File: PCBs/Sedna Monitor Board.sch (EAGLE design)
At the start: 39 parts, among them J1 uC Connection

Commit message: Started working on the Monitor Board layout
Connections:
- net N$24: now also ADC.CH4; no longer ADC.CH1
- net N$4: now also ADC.CH0; no longer ADC.CH4
- net N$5: now also ADC.CH1; no longer ADC.CH0
- net N$8: now also ADC.CH3; no longer ADC.CH2
- net N$9: now also ADC.CH2; no longer ADC.CH3
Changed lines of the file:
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@@
 </instance>
 <instance part="GND1" gate="1" x="132.08" y="127" smashed="yes"/>
-<instance part="GND2" gate="1" x="116.84" y="101.6" smashed="yes"/>
+<instance part="GND2" gate="1" x="114.3" y="104.14" smashed="yes"/>
 <instance part="C5" gate="G$1" x="157.48" y="83.82" smashed="yes">
 <attribute name="NAME" x="156.21" y="87.503" size="1.778" layer="95"/>
@@
 <segment>
 <pinref part="TEMP_SENSE" gate="G$1" pin="VSS"/>
-<wire x1="119.38" y1="109.22" x2="116.84" y2="109.22" width="0.1524" layer="91"/>
-<wire x1="116.84" y1="109.22" x2="116.84" y2="104.14" width="0.1524" layer="91"/>
-<wire x1="116.84" y1="99.06" x2="116.84" y2="104.14" width="0.1524" layer="91"/>
+<wire x1="119.38" y1="109.22" x2="114.3" y2="109.22" width="0.1524" layer="91"/>
+<wire x1="114.3" y1="109.22" x2="114.3" y2="106.68" width="0.1524" layer="91"/>
 <pinref part="GND2" gate="1" pin="GND"/>
 </segment>
@@
 <segment>
 <pinref part="CURRENT_SENSE" gate="G$1" pin="OUT"/>
-<wire x1="119.38" y1="137.16" x2="106.68" y2="137.16" width="0.1524" layer="91"/>
-<wire x1="106.68" y1="137.16" x2="106.68" y2="71.12" width="0.1524" layer="91"/>
-<pinref part="ADC" gate="MCP3208" pin="CH4"/>
-<wire x1="106.68" y1="71.12" x2="119.38" y2="71.12" width="0.1524" layer="91"/>
+<wire x1="119.38" y1="137.16" x2="109.22" y2="137.16" width="0.1524" layer="91"/>
+<pinref part="ADC" gate="MCP3208" pin="CH0"/>
+<wire x1="109.22" y1="137.16" x2="109.22" y2="81.28" width="0.1524" layer="91"/>
+<wire x1="109.22" y1="81.28" x2="119.38" y2="81.28" width="0.1524" layer="91"/>
 </segment>
 </net>
@@
 <junction x="165.1" y="111.76"/>
 <pinref part="V_BUFFER" gate="G$1" pin="VDD"/>
-<wire x1="58.42" y1="73.66" x2="50.8" y2="73.66" width="0.1524" layer="91"/>
-<wire x1="50.8" y1="73.66" x2="50.8" y2="48.26" width="0.1524" layer="91"/>
-<wire x1="50.8" y1="48.26" x2="165.1" y2="48.26" width="0.1524" layer="91"/>
+<wire x1="58.42" y1="73.66" x2="48.26" y2="73.66" width="0.1524" layer="91"/>
+<wire x1="48.26" y1="73.66" x2="48.26" y2="48.26" width="0.1524" layer="91"/>
+<wire x1="48.26" y1="48.26" x2="165.1" y2="48.26" width="0.1524" layer="91"/>
 <wire x1="165.1" y1="48.26" x2="165.1" y2="86.36" width="0.1524" layer="91"/>
 <pinref part="J1" gate="G$1" pin="VCC"/>
@@
 <wire x1="149.86" y1="73.66" x2="185.42" y2="73.66" width="0.1524" layer="91"/>
 <pinref part="TEMP_SENSE" gate="G$1" pin="SCK"/>
-<wire x1="119.38" y1="106.68" x2="111.76" y2="106.68" width="0.1524" layer="91"/>
-<wire x1="111.76" y1="106.68" x2="111.76" y2="93.98" width="0.1524" layer="91"/>
-<wire x1="111.76" y1="93.98" x2="185.42" y2="93.98" width="0.1524" layer="91"/>
-<wire x1="185.42" y1="93.98" x2="185.42" y2="114.3" width="0.1524" layer="91"/>
+<wire x1="119.38" y1="106.68" x2="116.84" y2="106.68" width="0.1524" layer="91"/>
+<wire x1="116.84" y1="106.68" x2="116.84" y2="96.52" width="0.1524" layer="91"/>
+<wire x1="116.84" y1="96.52" x2="185.42" y2="96.52" width="0.1524" layer="91"/>
+<wire x1="185.42" y1="96.52" x2="185.42" y2="114.3" width="0.1524" layer="91"/>
 <wire x1="185.42" y1="114.3" x2="208.28" y2="114.3" width="0.1524" layer="91"/>
-<wire x1="185.42" y1="73.66" x2="185.42" y2="93.98" width="0.1524" layer="91"/>
-<junction x="185.42" y="93.98"/>
+<wire x1="185.42" y1="73.66" x2="185.42" y2="96.52" width="0.1524" layer="91"/>
+<junction x="185.42" y="96.52"/>
 <pinref part="J1" gate="G$1" pin="SCK"/>
 </segment>
@@
 <pinref part="TEMP_SENSE" gate="G$1" pin="SI/O"/>
 <wire x1="139.7" y1="106.68" x2="142.24" y2="106.68" width="0.1524" layer="91"/>
-<wire x1="142.24" y1="106.68" x2="142.24" y2="91.44" width="0.1524" layer="91"/>
-<wire x1="142.24" y1="91.44" x2="187.96" y2="91.44" width="0.1524" layer="91"/>
-<wire x1="187.96" y1="91.44" x2="187.96" y2="111.76" width="0.1524" layer="91"/>
+<wire x1="142.24" y1="106.68" x2="142.24" y2="99.06" width="0.1524" layer="91"/>
+<wire x1="142.24" y1="99.06" x2="187.96" y2="99.06" width="0.1524" layer="91"/>
+<wire x1="187.96" y1="99.06" x2="187.96" y2="111.76" width="0.1524" layer="91"/>
 <wire x1="187.96" y1="111.76" x2="208.28" y2="111.76" width="0.1524" layer="91"/>
 <pinref part="ADC" gate="MCP3208" pin="D_OUT"/>
 <wire x1="149.86" y1="71.12" x2="187.96" y2="71.12" width="0.1524" layer="91"/>
-<wire x1="187.96" y1="71.12" x2="187.96" y2="91.44" width="0.1524" layer="91"/>
-<junction x="187.96" y="91.44"/>
+<wire x1="187.96" y1="71.12" x2="187.96" y2="99.06" width="0.1524" layer="91"/>
+<junction x="187.96" y="99.06"/>
 <pinref part="J1" gate="G$1" pin="MISO"/>
 </segment>
@@
 <segment>
 <pinref part="TEMP_SENSE" gate="G$1" pin="!CS"/>
-<wire x1="119.38" y1="111.76" x2="116.84" y2="111.76" width="0.1524" layer="91"/>
-<wire x1="116.84" y1="111.76" x2="116.84" y2="119.38" width="0.1524" layer="91"/>
-<wire x1="116.84" y1="119.38" x2="208.28" y2="119.38" width="0.1524" layer="91"/>
+<wire x1="119.38" y1="111.76" x2="114.3" y2="111.76" width="0.1524" layer="91"/>
+<wire x1="114.3" y1="111.76" x2="114.3" y2="119.38" width="0.1524" layer="91"/>
+<wire x1="114.3" y1="119.38" x2="208.28" y2="119.38" width="0.1524" layer="91"/>
 <pinref part="J1" gate="G$1" pin="!TEMP_CS"/>
 </segment>
@@
 <pinref part="V_BUFFER" gate="G$1" pin="VOUT_A"/>
 <wire x1="58.42" y1="81.28" x2="55.88" y2="81.28" width="0.1524" layer="91"/>
-<wire x1="55.88" y1="81.28" x2="55.88" y2="88.9" width="0.1524" layer="91"/>
-<wire x1="55.88" y1="88.9" x2="116.84" y2="88.9" width="0.1524" layer="91"/>
-<wire x1="116.84" y1="88.9" x2="116.84" y2="81.28" width="0.1524" layer="91"/>
-<pinref part="ADC" gate="MCP3208" pin="CH0"/>
-<wire x1="116.84" y1="81.28" x2="119.38" y2="81.28" width="0.1524" layer="91"/>
 <wire x1="55.88" y1="81.28" x2="55.88" y2="78.74" width="0.1524" layer="91"/>
 <junction x="55.88" y="81.28"/>
@@
 <wire x1="40.64" y1="124.46" x2="55.88" y2="124.46" width="0.1524" layer="91"/>
 <wire x1="55.88" y1="124.46" x2="55.88" y2="88.9" width="0.1524" layer="91"/>
+<pinref part="ADC" gate="MCP3208" pin="CH1"/>
+<wire x1="55.88" y1="88.9" x2="55.88" y2="81.28" width="0.1524" layer="91"/>
+<wire x1="119.38" y1="78.74" x2="101.6" y2="78.74" width="0.1524" layer="91"/>
+<wire x1="101.6" y1="78.74" x2="101.6" y2="88.9" width="0.1524" layer="91"/>
+<wire x1="101.6" y1="88.9" x2="55.88" y2="88.9" width="0.1524" layer="91"/>
 <junction x="55.88" y="88.9"/>
 </segment>
@@
 <wire x1="88.9" y1="66.04" x2="91.44" y2="66.04" width="0.1524" layer="91"/>
 <wire x1="91.44" y1="66.04" x2="111.76" y2="66.04" width="0.1524" layer="91"/>
-<wire x1="111.76" y1="66.04" x2="111.76" y2="76.2" width="0.1524" layer="91"/>
-<pinref part="ADC" gate="MCP3208" pin="CH2"/>
-<wire x1="111.76" y1="76.2" x2="119.38" y2="76.2" width="0.1524" layer="91"/>
 <pinref part="V_BUFFER" gate="G$1" pin="VIN_C-"/>
 <wire x1="88.9" y1="68.58" x2="91.44" y2="68.58" width="0.1524" layer="91"/>
@@
 <wire x1="40.64" y1="30.48" x2="91.44" y2="30.48" width="0.1524" layer="91"/>
 <wire x1="91.44" y1="30.48" x2="91.44" y2="66.04" width="0.1524" layer="91"/>
+<wire x1="111.76" y1="66.04" x2="111.76" y2="73.66" width="0.1524" layer="91"/>
+<pinref part="ADC" gate="MCP3208" pin="CH3"/>
+<wire x1="119.38" y1="73.66" x2="111.76" y2="73.66" width="0.1524" layer="91"/>
 </segment>
 </net>
@@
 <pinref part="V_BUFFER" gate="G$1" pin="VOUT_D"/>
 <wire x1="88.9" y1="81.28" x2="91.44" y2="81.28" width="0.1524" layer="91"/>
-<wire x1="91.44" y1="81.28" x2="109.22" y2="81.28" width="0.1524" layer="91"/>
-<wire x1="109.22" y1="81.28" x2="109.22" y2="73.66" width="0.1524" layer="91"/>
-<pinref part="ADC" gate="MCP3208" pin="CH3"/>
-<wire x1="109.22" y1="73.66" x2="119.38" y2="73.66" width="0.1524" layer="91"/>
 <pinref part="V_BUFFER" gate="G$1" pin="VIN_D-"/>
 <wire x1="88.9" y1="78.74" x2="91.44" y2="78.74" width="0.1524" layer="91"/>
@@
 <wire x1="91.44" y1="124.46" x2="91.44" y2="81.28" width="0.1524" layer="91"/>
 <junction x="91.44" y="81.28"/>
+<pinref part="ADC" gate="MCP3208" pin="CH2"/>
+<wire x1="119.38" y1="76.2" x2="99.06" y2="76.2" width="0.1524" layer="91"/>
+<wire x1="99.06" y1="76.2" x2="99.06" y2="81.28" width="0.1524" layer="91"/>
+<wire x1="99.06" y1="81.28" x2="91.44" y2="81.28" width="0.1524" layer="91"/>
 </segment>
 </net>
 <net name="N$12" class="0">
 <segment>
-<wire x1="53.34" y1="114.3" x2="53.34" y2="76.2" width="0.1524" layer="91"/>
+<wire x1="48.26" y1="114.3" x2="48.26" y2="76.2" width="0.1524" layer="91"/>
 <pinref part="V_BUFFER" gate="G$1" pin="VIN_A+"/>
-<wire x1="53.34" y1="76.2" x2="58.42" y2="76.2" width="0.1524" layer="91"/>
+<wire x1="48.26" y1="76.2" x2="58.42" y2="76.2" width="0.1524" layer="91"/>
 <pinref part="CFILT2_VIN" gate="G$1" pin="2"/>
 <junction x="30.48" y="114.3"/>
 <pinref part="RFILT2_VIN" gate="G$1" pin="1"/>
-<wire x1="53.34" y1="114.3" x2="30.48" y2="114.3" width="0.1524" layer="91"/>
+<wire x1="48.26" y1="114.3" x2="30.48" y2="114.3" width="0.1524" layer="91"/>
 </segment>
 </net>
@@
 <wire x1="55.88" y1="66.04" x2="55.88" y2="58.42" width="0.1524" layer="91"/>
 <wire x1="55.88" y1="58.42" x2="114.3" y2="58.42" width="0.1524" layer="91"/>
-<pinref part="ADC" gate="MCP3208" pin="CH1"/>
-<wire x1="114.3" y1="58.42" x2="114.3" y2="78.74" width="0.1524" layer="91"/>
-<wire x1="114.3" y1="78.74" x2="119.38" y2="78.74" width="0.1524" layer="91"/>
 <pinref part="V_BUFFER" gate="G$1" pin="VIN_B-"/>
 <wire x1="58.42" y1="68.58" x2="55.88" y2="68.58" width="0.1524" layer="91"/>
@@
 <wire x1="43.18" y1="68.58" x2="55.88" y2="68.58" width="0.1524" layer="91"/>
 <junction x="55.88" y="68.58"/>
-</segment>
-</net>
+<wire x1="114.3" y1="58.42" x2="114.3" y2="71.12" width="0.1524" layer="91"/>
+<pinref part="ADC" gate="MCP3208" pin="CH4"/>
+<wire x1="119.38" y1="71.12" x2="114.3" y2="71.12" width="0.1524" layer="91"/>
+</segment>
+</net>

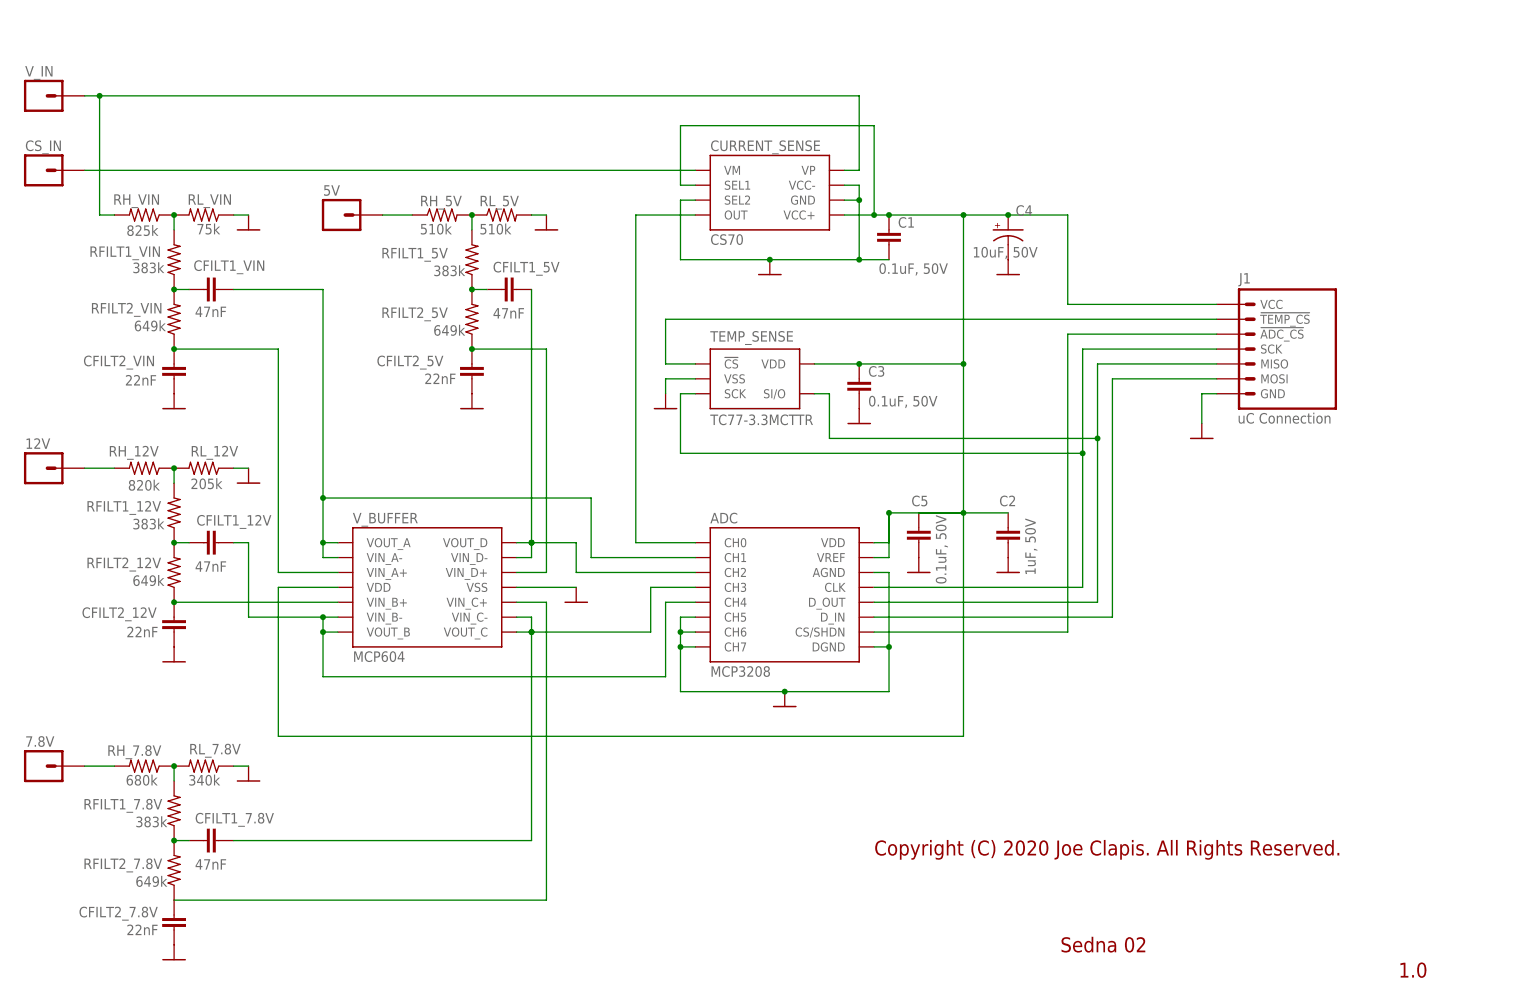
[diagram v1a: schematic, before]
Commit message: Finished the Monitor Board v1.0
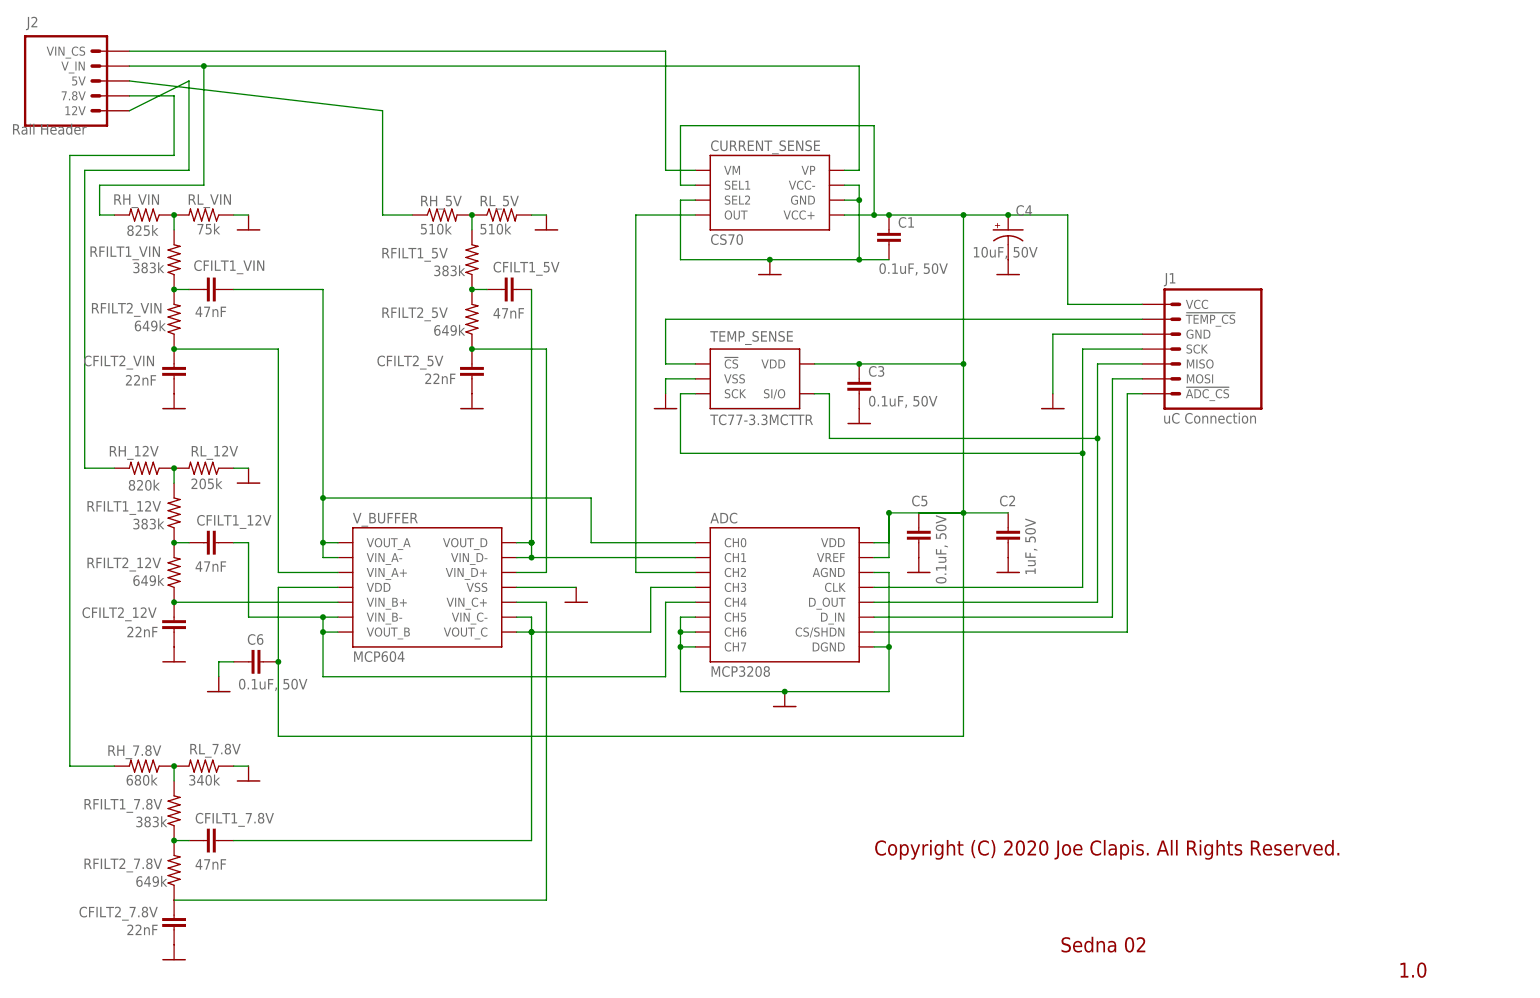
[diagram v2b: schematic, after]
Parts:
- removed 12V, 5V, 7.8V, CS_IN, V_IN: (no value), SparkFun-Connectors:M01PTH
- added C6: 0.1uF, 50V, rcl:C-EUC0805
- added J2: Rail Header, Sedna Components:RAIL_HEADER
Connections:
- net N$24 renamed VOUT_B
- net N$6 renamed MOSI
- net N$8 renamed VOUT_C
- removed net N$20: 7.8V.1, RH_7.8V.2
- removed net N$5: ADC.CH1, CFILT1_VIN.2, V_BUFFER.VIN_A-, V_BUFFER.VOUT_A
- removed net N$9: ADC.CH2, CFILT1_5V.1, V_BUFFER.VIN_D-, V_BUFFER.VOUT_D
- new net CS_OUT: ADC.CH2, CURRENT_SENSE.OUT
- new net VOUT_A: ADC.CH0, CFILT1_VIN.2, V_BUFFER.VIN_A-, V_BUFFER.VOUT_A
- new net VOUT_D: ADC.CH1, CFILT1_5V.1, V_BUFFER.VIN_D-, V_BUFFER.VOUT_D
- net GND: now also C6.2
- net N$10: now also J2.5V; no longer 5V.1
- net N$14: now also J2.12V; no longer 12V.1
- net N$2: now also J2.VIN_CS; no longer CS_IN.1
- net N$3: now also J2.V_IN; no longer V_IN.1
- net N$4: now also J2.7.8V, RH_7.8V.2; no longer ADC.CH0, CURRENT_SENSE.OUT
- net VDD: now also C6.1
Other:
- moved on the sheet: J1
